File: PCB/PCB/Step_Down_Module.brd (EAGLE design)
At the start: 55.6 x 97.2 mm, 48 parts, among them J1 JUMPER-SMT_3_1-NC_PASTE_SILK, J2 JUMPER-SMT_3_1-NC_PASTE_SILK, J7 JUMPER-SMT_3_1-NC_PASTE_SILK, Q1 FDMC86240, Q2 FDMC86240, Q3 TPH2900ENH, U1 LTC3895_STEP_DOWN_DC-DC_CONVE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

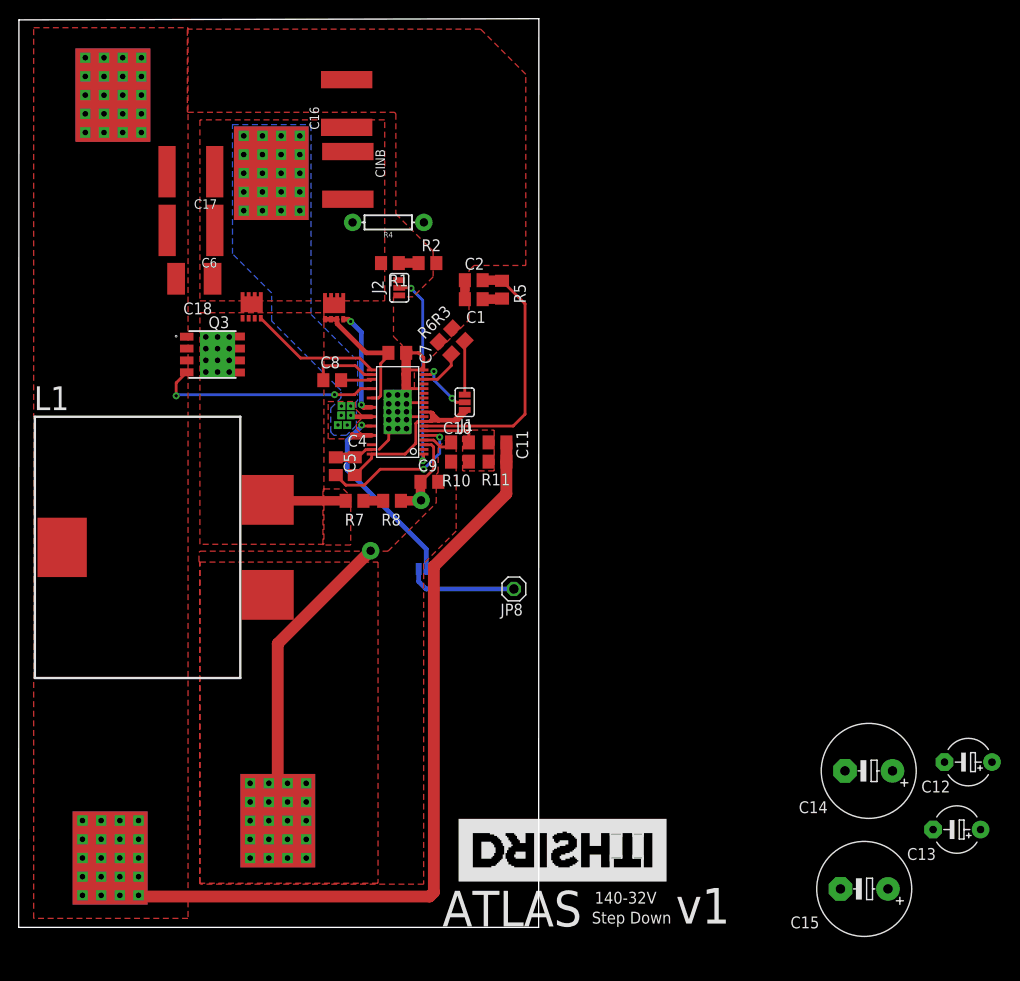
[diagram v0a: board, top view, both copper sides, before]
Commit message: WIP-PCB revision 2; Major parts of layout done
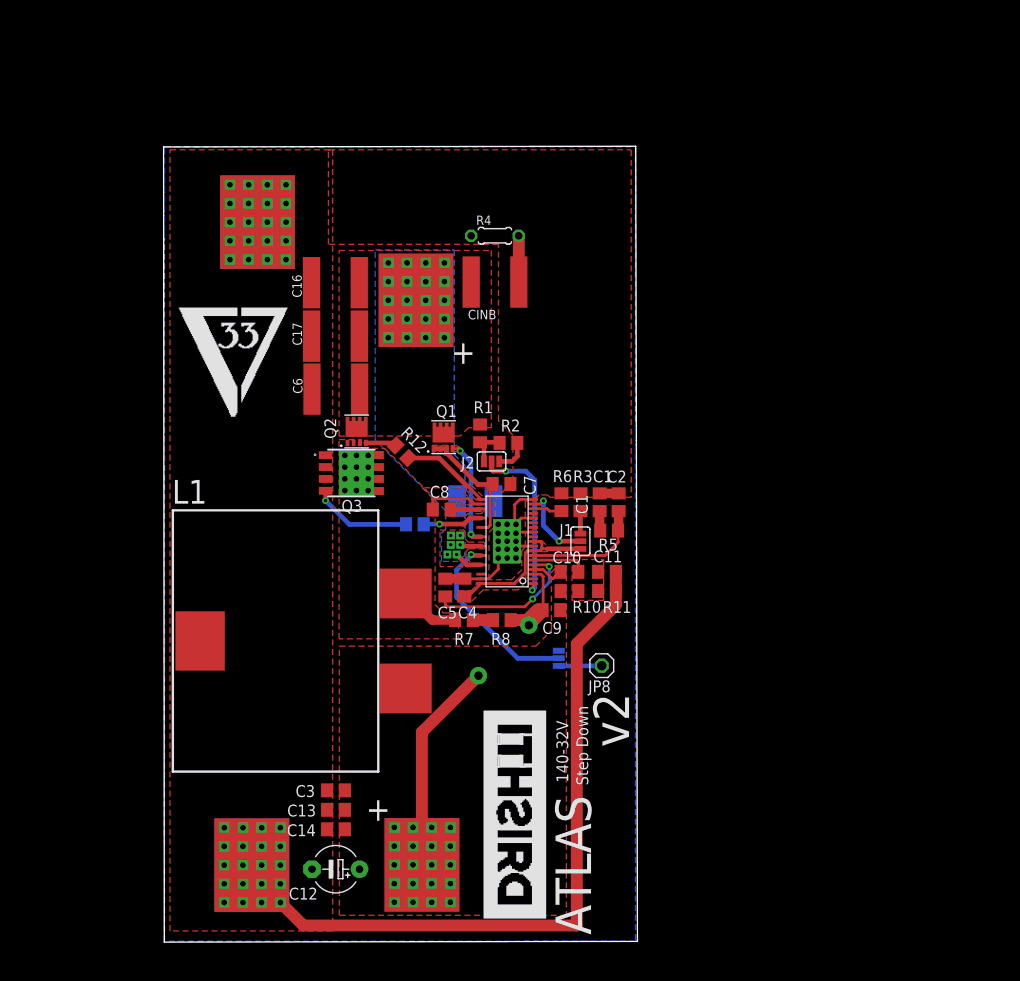
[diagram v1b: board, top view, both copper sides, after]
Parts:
- removed C15: 150uF, rcl:E5-10,5
- added C3: (no value), rcl:C0805
- added R12, R13: (no value), rcl:R0805
- C13: value 22uF -> (none); device rcl:E5-5 -> rcl:C0805
- C14: value 150uF -> (none); device rcl:E5-10,5 -> rcl:C0805
- R4: device SparkFun-Resistors:AXIAL-0.3 -> resistor:0204/5
- moved C12 68.6 mm to (18.3, 7.80)
- moved C13 66.4 mm to (18.4, 14.1)
- moved C14 57.3 mm to (18.4, 12.1)
- moved C18 38.3 mm to (33.3, 47.1), flipped to the bottom
- moved C2 28.4 mm to (48.6, 47.0), turned to 90 degrees
- moved R5 28.2 mm to (47.6, 44.0), turned to 180 degrees
- moved C1 25.6 mm to (46.6, 47.0), turned to 90 degrees
- moved C17 23.4 mm to (18.3, 64.8)
- moved C6 23.0 mm to (18.3, 59.1)
- moved R3 22.2 mm to (44.5, 47.0), turned to 90 degrees
- moved R2 21.1 mm to (36.8, 53.4)
- moved J2 21.0 mm to (35.0, 51.4), turned to 180 degrees
- moved R6 20.7 mm to (42.5, 47.0), turned to 270 degrees
- moved R1 20.6 mm to (33.8, 54.4), turned to 270 degrees
- moved VIN_NEG 20.6 mm to (10.1, 77.5)
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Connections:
- new net N$2: Q2.G, R12.1
- new net N$3: Q3.G, R13.1
- net G2: now also R12.2; no longer Q2.G
- net G3: now also R13.2; no longer Q3.G
- net GND: now also C13.2, C14.2, C3.2, R4.1; no longer C13.-, C14.-, C15.-, R4.P$1
- net N$1: now also R4.2; no longer R4.P$2
- net VOUT: now also C13.1, C14.1, C3.1; no longer C13.+, C14.+, C15.+
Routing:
- net G3: track 24.2 -> 6.42 mm, vias 2 -> 1
- net ITH: track 28.9 -> 13.1 mm
- net GND: track 134.8 -> 122.4 mm
- net N$3: track 0.00 -> 10.7 mm, vias 0 -> 1
- net VOUT: track 36.4 -> 26.4 mm
- net N$13: track 11.9 -> 4.61 mm
- net N$1: track 0.00 -> 4.96 mm
- net G2: track 14.1 -> 9.63 mm
- net INTVCC: track 21.6 -> 17.4 mm
- net N$5: track 5.75 -> 2.41 mm
- net N$2: track 0.00 -> 3.31 mm
- net N$6: track 9.94 -> 13.1 mm
- net SW: track 15.5 -> 13.1 mm
- net OVLO: track 21.0 -> 18.6 mm
- net N$9: track 2.11 -> 4.32 mm
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- added copper zone on layer 1, net BOOST
- added copper zone on layer 1, net DRVCC
- added copper zone on layer 1, net G2
- added copper zone on layer 16, net GND
- added copper zone on layer 1, net INTVCC
- added copper zone on layer 1, net NDRV
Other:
- board size 55.6 x 97.2 mm -> 50.7 x 85.1 mm
- board text added: "+"
- board text added: "C1"
- board text added: "Q1"
- board text added: "Q2"
- board text added: "v2"
- board text removed: "v1"

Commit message: WIP:PCB revision 2; Move inductor and optimize SW Node area
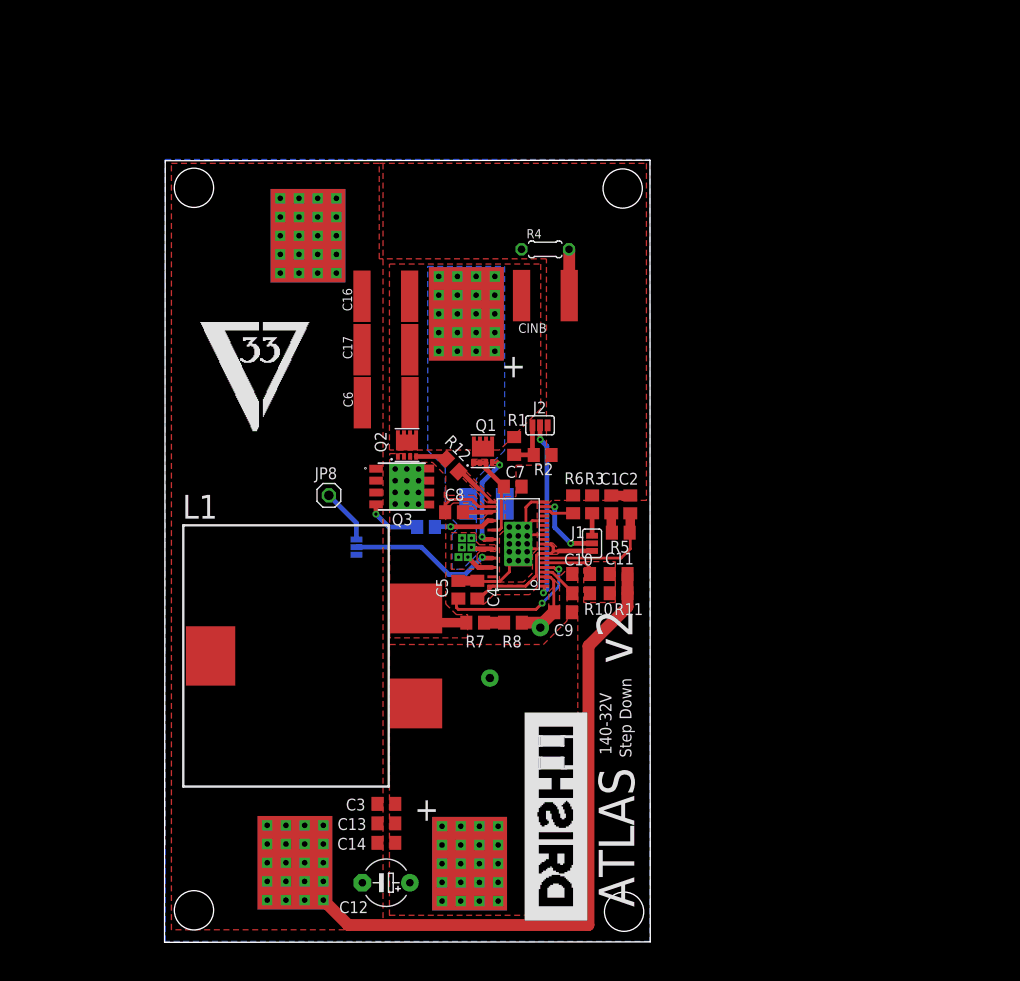
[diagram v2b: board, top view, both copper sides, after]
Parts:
- moved JP8 34.4 mm to (17.6, 47.8)
- moved J7 24.7 mm to (20.5, 42.2), turned to 270 degrees
- moved J2 6.46 mm to (40.2, 55.3)
- moved C12 5.58 mm to (23.7, 6.35)
- moved C16 5.58 mm to (23.7, 69.1)
- moved Q3 5.58 mm to (24.7, 50.6)
- moved VIN_POS 5.58 mm to (32.4, 67.7)
- moved VIN_NEG 5.58 mm to (15.5, 76.0)
- moved C13 5.58 mm to (23.7, 12.7)
- moved C17 5.58 mm to (23.7, 63.4)
- moved C6 5.58 mm to (23.7, 57.7)
- moved CINB 5.58 mm to (40.8, 69.1)
- moved Q2 5.58 mm to (26.0, 53.0)
- moved R12 5.58 mm to (30.8, 51.0)
- moved C14 5.58 mm to (23.7, 10.6)
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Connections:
- net N$6 renamed S+
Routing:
- net VOUT: track 26.4 -> 4.09 mm
- net GND: track 122.4 -> 115.2 mm
- net G2: track 9.63 -> 4.96 mm
- net N$3: track 10.7 -> 6.03 mm
- net S+: track 13.1 -> 9.14 mm
- net DRVCC: track 13.6 -> 10.2 mm
- net EXTVCC: track 20.0 -> 16.6 mm
- net N$13: track 4.61 -> 5.94 mm
- net N$9: track 4.32 -> 5.34 mm
- net NDRV: track 11.5 -> 10.6 mm
- net SW: track 13.1 -> 12.4 mm
- net OVLO: track 18.6 -> 19.1 mm
- net DRVSET: track 8.55 -> 8.03 mm
- added copper zone on layer 1, net S+
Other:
- board size 50.7 x 85.1 mm -> 51.9 x 83.6 mm
- board text removed: "C1"

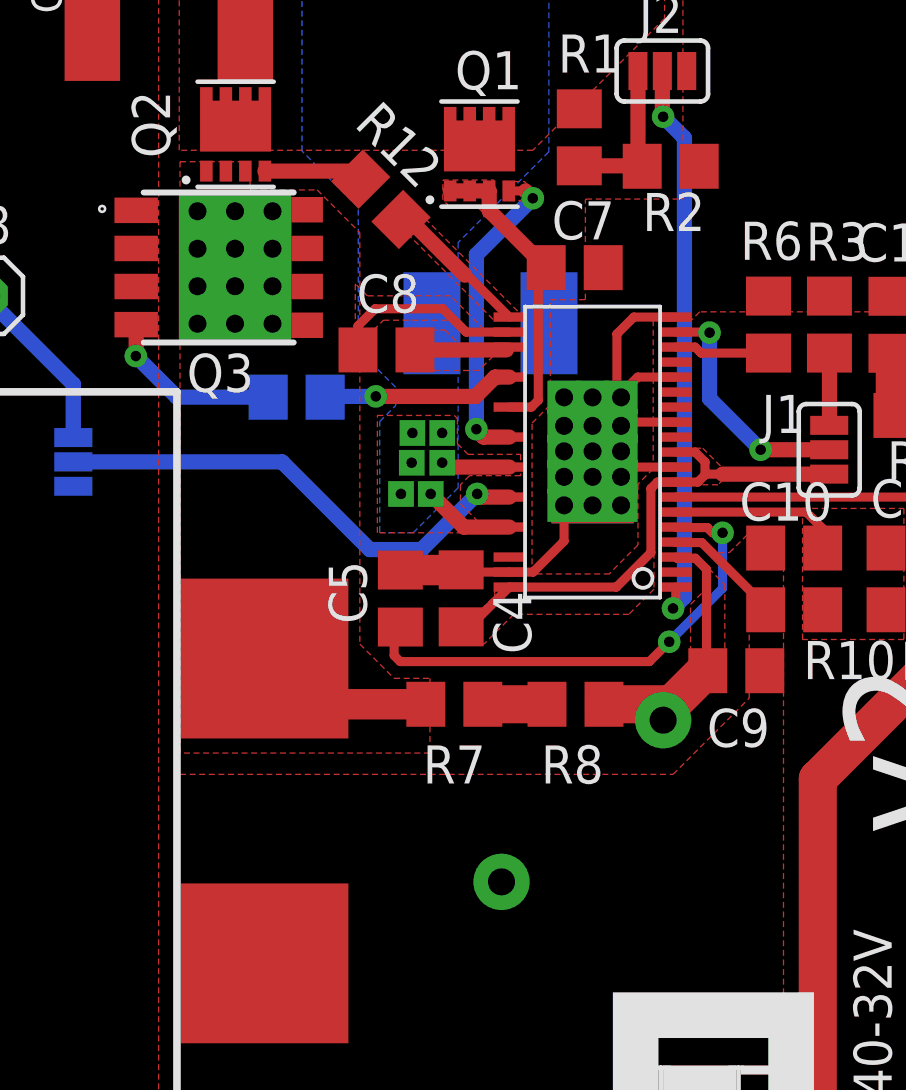
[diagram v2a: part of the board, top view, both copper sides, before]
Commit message: Corrected sense resistors, DRVCC trace
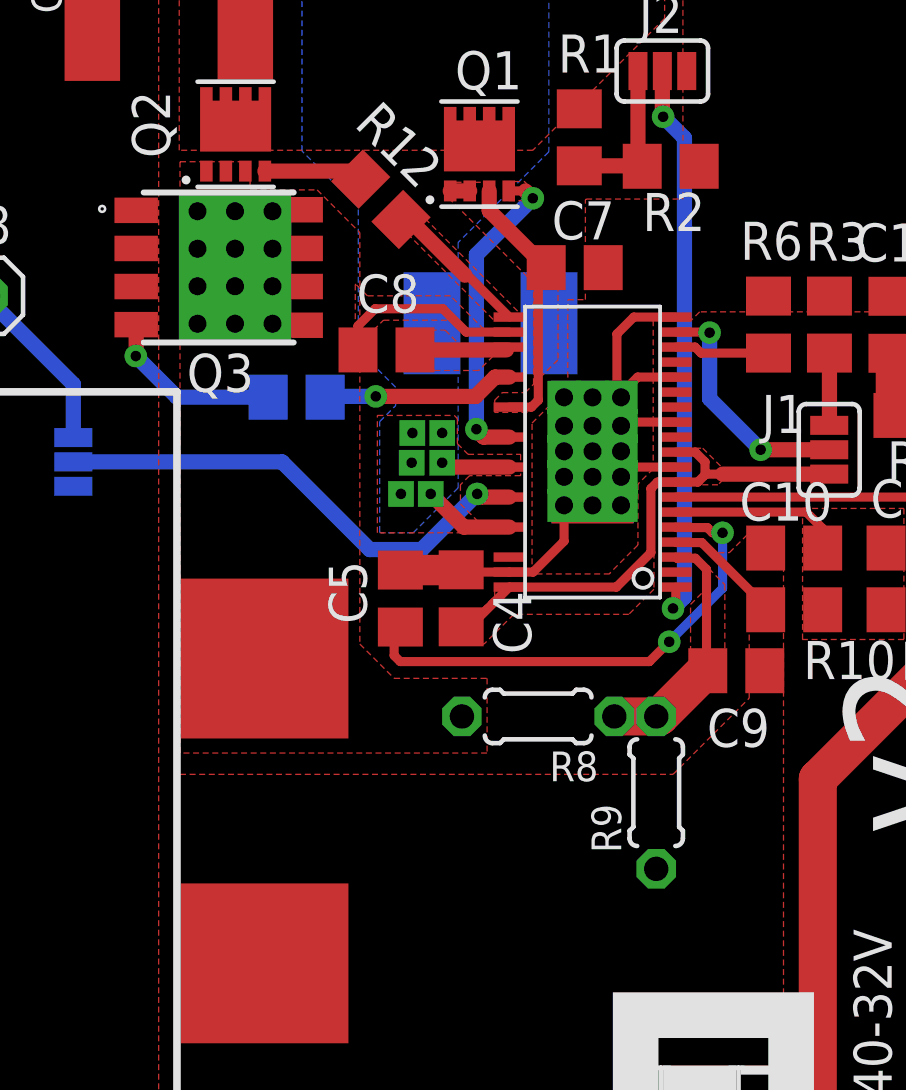
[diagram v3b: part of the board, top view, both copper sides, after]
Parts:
- removed R7: 270k, rcl:R0805
- C12: value 22uF -> (none)
- C9: value 0.01uF -> 1uF
- R8: value 10k -> 3.9k; device rcl:R0805 -> resistor:0204/5
- R9: value 10000k -> 12k; device SparkFun-Resistors:AXIAL-0.3 -> resistor:0204/5
- moved R9 2.48 mm to (40.0, 31.2), flipped to the top, turned to 90 degrees
- moved R8 1.31 mm to (36.0, 33.8)
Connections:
- removed net N$7: R7.1, R8.2
- net S+: now also R9.2; no longer R9.P$1
- net SW: now also R8.2; no longer R7.2
- net VOUT: now also R9.1; no longer R9.P$2
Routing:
- net SW: track 12.4 -> 6.40 mm
- net N$7: track 2.14 -> 0.00 mm
- net S+: track 9.14 -> 8.31 mm
- net DRVCC: track 10.2 -> 9.58 mm

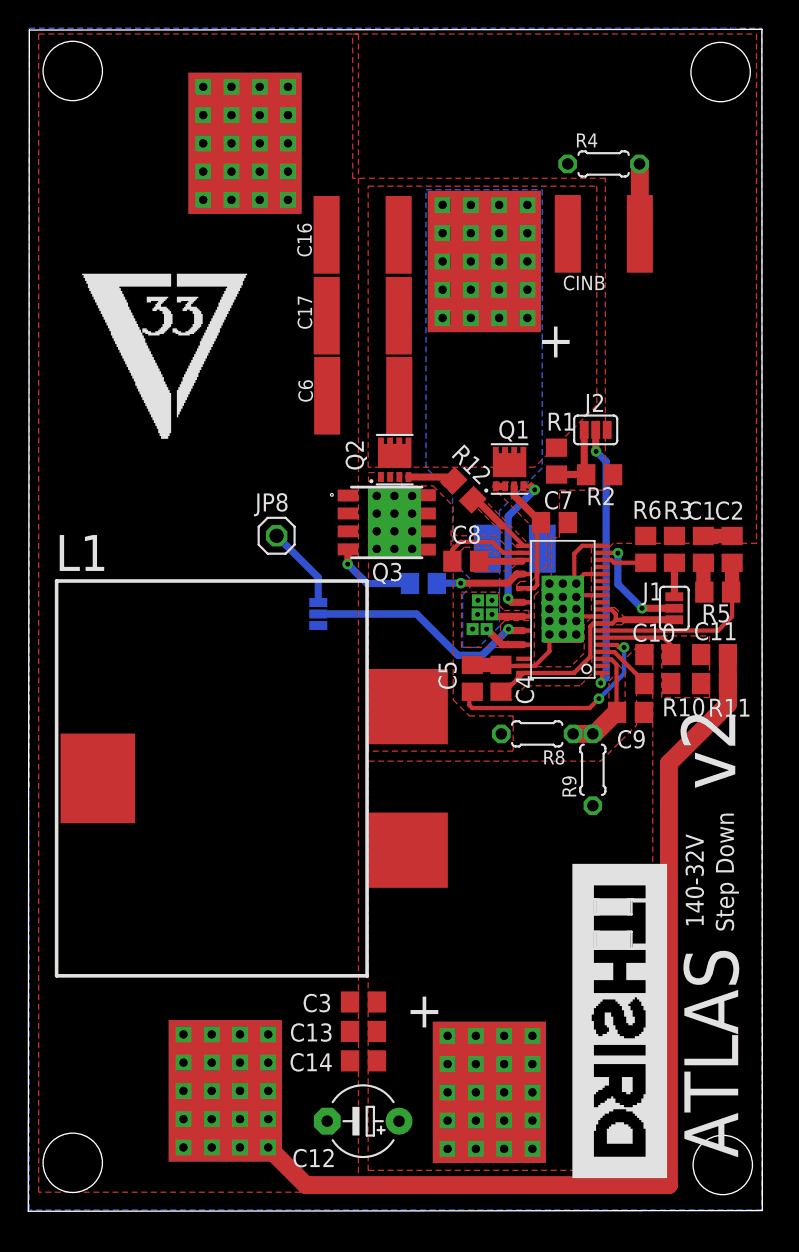
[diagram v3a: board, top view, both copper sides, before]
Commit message: Added electrolytics, test points
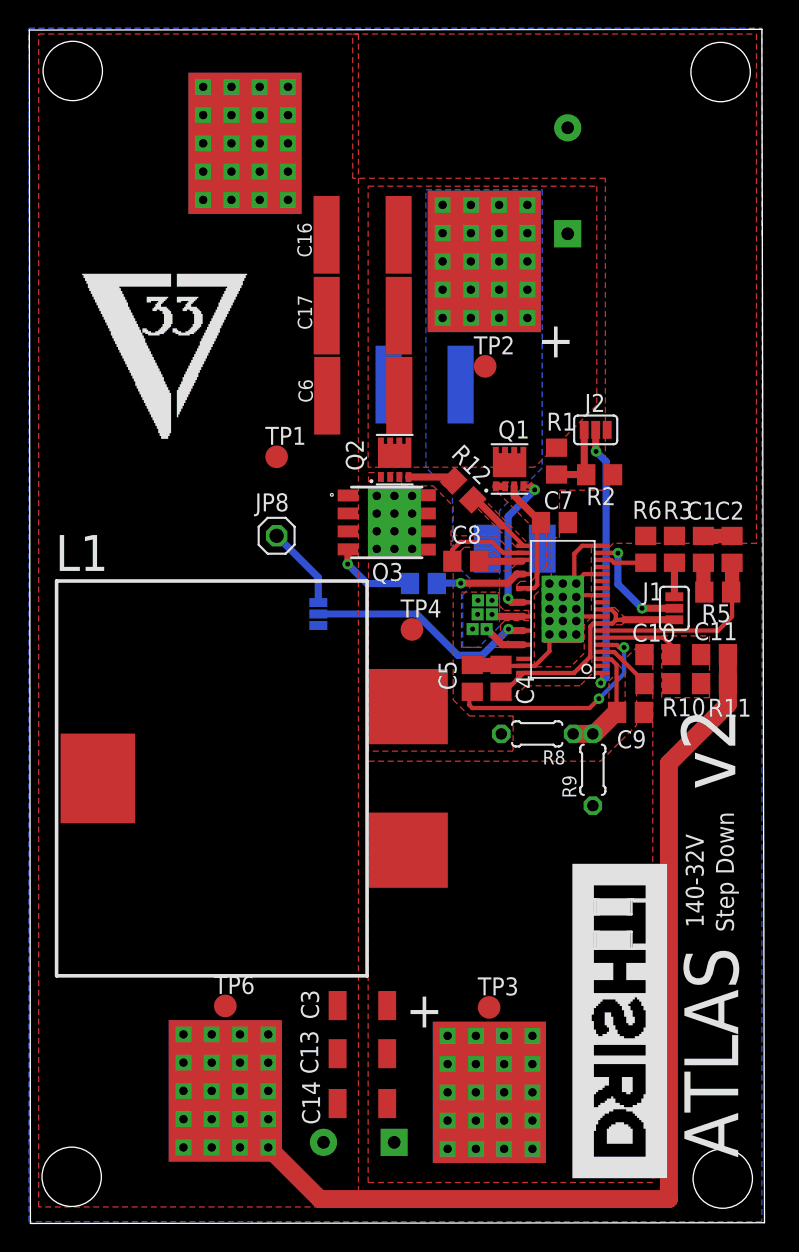
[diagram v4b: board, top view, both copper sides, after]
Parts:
- removed R4: 100, resistor:0204/5
- added C15: 220U, SparkFun-Capacitors:CPOL-RADIAL-7.5MM-18MM
- added TP1, TP2, TP3, TP4, TP6: TPTP16R, testpad:TP16R
- C12: value (none) -> 220u; device rcl:E5-5 -> SparkFun-Capacitors:CPOL-RADIAL-5MM-10MM
- C13, C14, C3: value (none) -> 10u; device rcl:C0805 -> SparkFun-Capacitors:1210
- moved CINB 16.6 mm to (28.1, 58.5), flipped to the bottom
- moved C14 3.02 mm to (23.7, 7.59)
- moved C13 1.58 mm to (23.7, 11.1)
- moved C12 1.53 mm to (23.4, 4.85), flipped to the bottom
- moved C3 0.27 mm to (23.7, 14.5)
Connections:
- removed net N$1: CINB.2, R4.2
- net GND: now also C15.-, CINB.2, TP1.TP, TP6.TP; no longer R4.1
- net SW: now also TP4.TP
- net VIN: now also C15.+, TP2.TP
- net VOUT: now also TP3.TP
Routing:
- net N$1: track 4.96 -> 0.00 mm
- net GND: track 115.2 -> 116.6 mm
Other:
- board size 51.9 x 83.6 mm -> 52 x 84.5 mm

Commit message: PCB rev2 sent for manufacture
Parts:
- added C19: 10u, SparkFun-Capacitors:1210
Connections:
- net GND: now also C19.2
- net SW: now also Q3.D1
- net VOUT: now also C19.1
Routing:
- added copper zone on layer 16, net VOUT
